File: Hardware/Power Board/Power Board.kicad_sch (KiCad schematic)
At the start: 15 parts, among them IC1 SN6507DGQR, T1 782100_35JVC

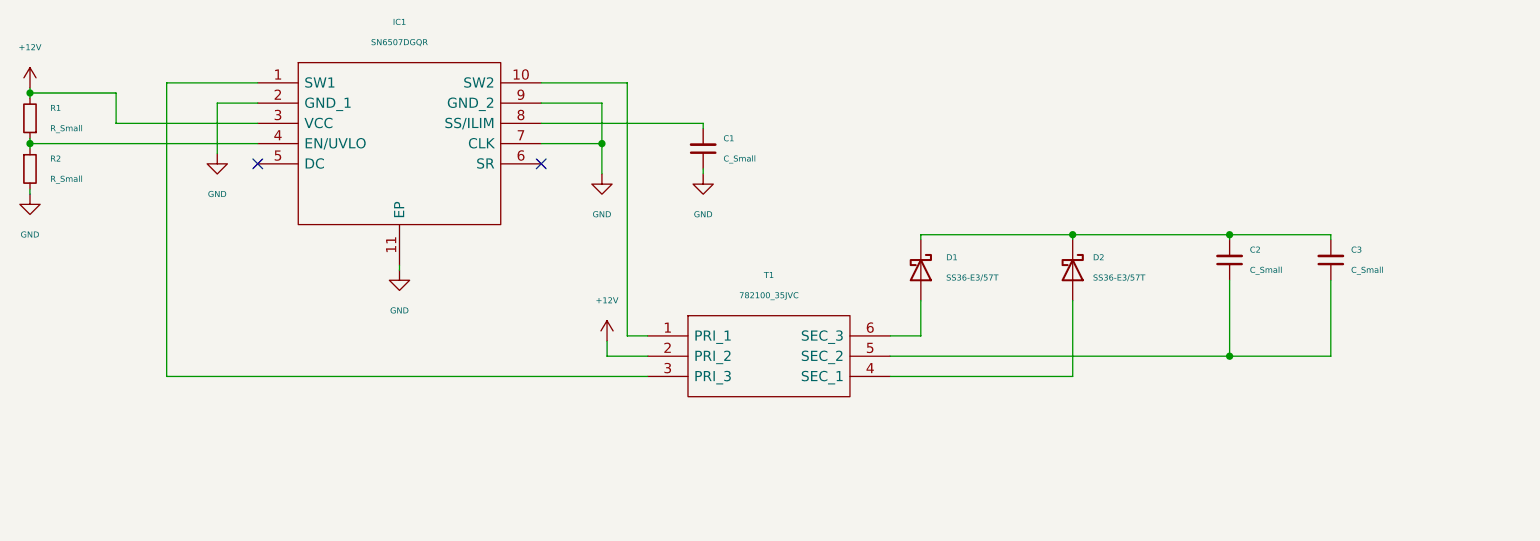
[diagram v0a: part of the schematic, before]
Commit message: Updates to board, changed gate driver IC to one with external clamp
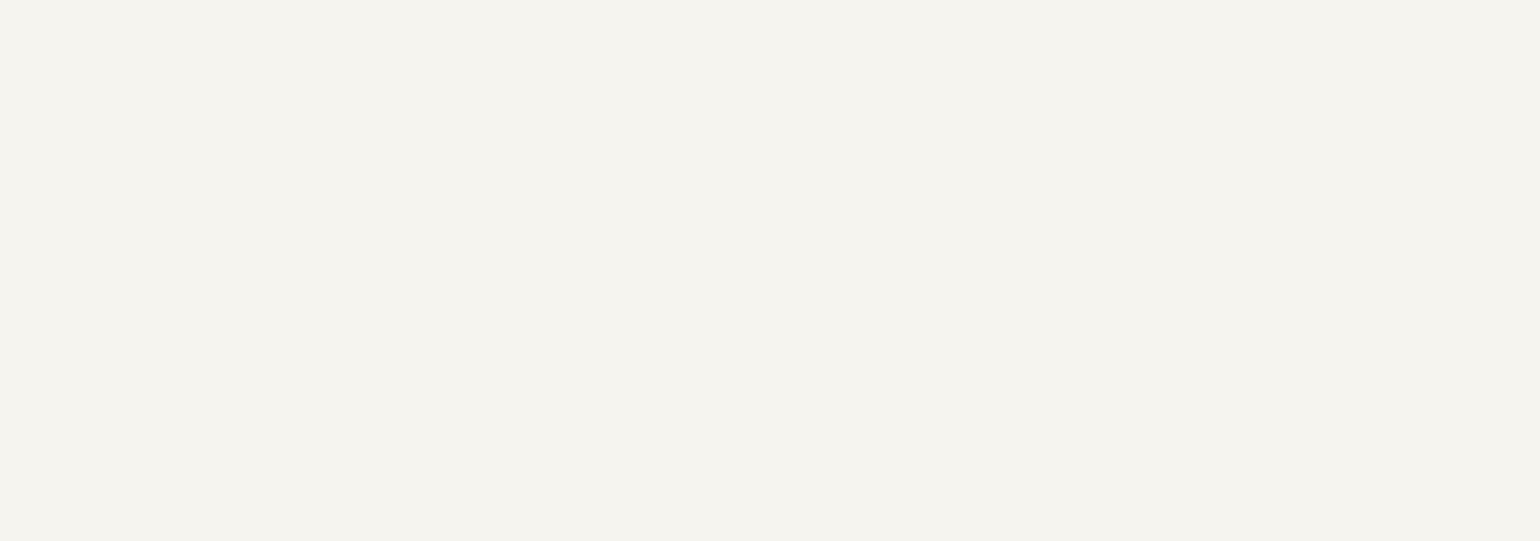
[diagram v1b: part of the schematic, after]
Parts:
- removed C1, C2, C3: C_Small, symbol Device:C_Small
- removed D1, D2: SS36-E3/57T, Diode_SMD:D_SMC, symbol Device:D_Schottky
- removed IC1: SN6507DGQR, SOP50P490X110-11N, symbol SamacSys_Parts:SN6507DGQR
- removed R1, R2: R_Small, symbol Device:R_Small
- removed T1: 782100_35JVC, 78210035JVC, symbol SamacSys_Parts:782100_35JVC
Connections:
- no-connect marks 2 -> 0

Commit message: Ditched ASC
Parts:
- removed R3, R4, R5, R6, R7, R8: R_Small, symbol Device:R_Small
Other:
- sheet LOW_SIDE_POWER_STAGE renamed POWER_STAGE
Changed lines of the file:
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@@
     (company "Logan Rosenmayer")
-  )
-  (wire (pts (xy 71.755 260.985) (xy 71.755 262.255))
-    (stroke (width 0) (type default))
-  )
-  (wire (pts (xy 71.755 273.685) (xy 71.755 274.955))
-    (stroke (width 0) (type default))
-  )
-  (wire (pts (xy 71.755 254.635) (xy 71.755 255.905))
-    (stroke (width 0) (type default))
-  )
-  (wire (pts (xy 71.755 267.335) (xy 71.755 268.605))
-    (stroke (width 0) (type default))
-  )
-  (wire (pts (xy 71.755 248.285) (xy 71.755 249.555))
-    (stroke (width 0) (type default))
-  )
-  (global_label "HV +" (shape input) (at 71.755 243.205 90) (fields_autoplaced)
-    (effects (font (size 1.27 1.27)) (justify left))
-    (property "Intersheetrefs" "${INTERSHEET_REFS}" (at 71.6756 235.8329 90)
-      (effects (font (size 1.27 1.27)) (justify left) hide)
-    )
-  )
-  (global_label "HV -" (shape input) (at 71.755 280.035 270) (fields_autoplaced)
-    (effects (font (size 1.27 1.27)) (justify right))
-    (property "Intersheetrefs" "${INTERSHEET_REFS}" (at 71.6756 287.4071 90)
-      (effects (font (size 1.27 1.27)) (justify right) hide)
-    )
-  )
-  (symbol (lib_id "Device:R_Small") (at 71.755 258.445 180) (unit 1)
-    (in_bom yes) (on_board yes) (dnp no) (fields_autoplaced)
-    (property "Reference" "R5" (at 73.66 257.1749 0)
-      (effects (font (size 0.75 0.75)) (justify right))
-    )
-    (property "Value" "R_Small" (at 73.66 259.7149 0)
-      (effects (font (size 0.75 0.75)) (justify right))
-    )
-    (property "Footprint" "" (at 71.755 258.445 0)
-      (effects (font (size 1.27 1.27)) hide)
-    )
-    (property "Datasheet" "~" (at 71.755 258.445 0)
-      (effects (font (size 1.27 1.27)) hide)
-    )
-    (pin "1")
-    (pin "2")
-    (instances
-      (project "Power Board"
-        (path "/6be5afcf-5319-4edd-874e-36cb4fffe262"
-          (reference "R5") (unit 1)
-        )
-      )
-    )
-  )
-  (symbol (lib_id "Device:R_Small") (at 71.755 252.095 180) (unit 1)
-    (in_bom yes) (on_board yes) (dnp no) (fields_autoplaced)
-    (property "Reference" "R4" (at 73.66 250.8249 0)
-      (effects (font (size 0.75 0.75)) (justify right))
-    )
-    (property "Value" "R_Small" (at 73.66 253.3649 0)
-      (effects (font (size 0.75 0.75)) (justify right))
-    )
-    (property "Footprint" "" (at 71.755 252.095 0)
-      (effects (font (size 1.27 1.27)) hide)
-    )
-    (property "Datasheet" "~" (at 71.755 252.095 0)
-      (effects (font (size 1.27 1.27)) hide)
-    )
-    (pin "1")
-    (pin "2")
-    (instances
-      (project "Power Board"
-        (path "/6be5afcf-5319-4edd-874e-36cb4fffe262"
-          (reference "R4") (unit 1)
-        )
-      )
-    )
-  )
-  (symbol (lib_id "Device:R_Small") (at 71.755 245.745 180) (unit 1)
-    (in_bom yes) (on_board yes) (dnp no) (fields_autoplaced)
-    (property "Reference" "R3" (at 73.66 244.4749 0)
-      (effects (font (size 0.75 0.75)) (justify right))
-    )
-    (property "Value" "R_Small" (at 73.66 247.0149 0)
-      (effects (font (size 0.75 0.75)) (justify right))
-    )
-    (property "Footprint" "" (at 71.755 245.745 0)
-      (effects (font (size 1.27 1.27)) hide)
-    )
-    (property "Datasheet" "~" (at 71.755 245.745 0)
-      (effects (font (size 1.27 1.27)) hide)
-    )
-    (pin "1")
-    (pin "2")
-    (instances
-      (project "Power Board"
-        (path "/6be5afcf-5319-4edd-874e-36cb4fffe262"
-          (reference "R3") (unit 1)
-        )
-      )
-    )
-  )
-  (symbol (lib_id "Device:R_Small") (at 71.755 277.495 180) (unit 1)
-    (in_bom yes) (on_board yes) (dnp no) (fields_autoplaced)
-    (property "Reference" "R8" (at 74.295 276.2249 0)
-      (effects (font (size 0.75 0.75)) (justify right))
-    )
-    (property "Value" "R_Small" (at 74.295 278.7649 0)
-      (effects (font (size 0.75 0.75)) (justify right))
-    )
-    (property "Footprint" "" (at 71.755 277.495 0)
-      (effects (font (size 1.27 1.27)) hide)
-    )
-    (property "Datasheet" "~" (at 71.755 277.495 0)
-      (effects (font (size 1.27 1.27)) hide)
-    )
-    (pin "1")
-    (pin "2")
-    (instances
-      (project "Power Board"
-        (path "/6be5afcf-5319-4edd-874e-36cb4fffe262"
-          (reference "R8") (unit 1)
-        )
-      )
-    )
-  )
-  (symbol (lib_id "Device:R_Small") (at 71.755 271.145 180) (unit 1)
-    (in_bom yes) (on_board yes) (dnp no) (fields_autoplaced)
-    (property "Reference" "R7" (at 73.66 269.8749 0)
-      (effects (font (size 0.75 0.75)) (justify right))
-    )
-    (property "Value" "R_Small" (at 73.66 272.4149 0)
-      (effects (font (size 0.75 0.75)) (justify right))
-    )
-    (property "Footprint" "" (at 71.755 271.145 0)
-      (effects (font (size 1.27 1.27)) hide)
-    )
-    (property "Datasheet" "~" (at 71.755 271.145 0)
-      (effects (font (size 1.27 1.27)) hide)
-    )
-    (pin "1")
-    (pin "2")
-    (instances
-      (project "Power Board"
-        (path "/6be5afcf-5319-4edd-874e-36cb4fffe262"
-          (reference "R7") (unit 1)
-        )
-      )
-    )
-  )
-  (symbol (lib_id "Device:R_Small") (at 71.755 264.795 180) (unit 1)
-    (in_bom yes) (on_board yes) (dnp no) (fields_autoplaced)
-    (property "Reference" "R6" (at 73.66 263.5249 0)
-      (effects (font (size 0.75 0.75)) (justify right))
-    )
-    (property "Value" "R_Small" (at 73.66 266.0649 0)
-      (effects (font (size 0.75 0.75)) (justify right))
-    )
-    (property "Footprint" "" (at 71.755 264.795 0)
-      (effects (font (size 1.27 1.27)) hide)
-    )
-    (property "Datasheet" "~" (at 71.755 264.795 0)
-      (effects (font (size 1.27 1.27)) hide)
-    )
-    (pin "1")
-    (pin "2")
-    (instances
-      (project "Power Board"
-        (path "/6be5afcf-5319-4edd-874e-36cb4fffe262"
-          (reference "R6") (unit 1)
-        )
-      )
-    )
   )
   (sheet (at 200.66 203.2) (size 42.545 30.48) (fields_autoplaced)
     (stroke (width 0.1524) (type solid))
     (fill (color 0 0 0 0.0000))
-    (property "Sheetname" "LOW_SIDE_POWER_STAGE" (at 200.66 202.4884 0)
+    (property "Sheetname" "POWER_STAGE" (at 200.66 202.4884 0)
       (effects (font (size 1.27 1.27)) (justify left bottom))
     )

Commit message: Board Layout Almost Done, about to remove Kelvin source due to concerns about uneven current sharing
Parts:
- added C153, C154, C155, C156, C157, C158, C159, C160: 100uF-420V-20%-D16P7.5, Capacitor_THT:CP_Radial_D16.0mm_P7.50mm, symbol Device:C_Polarized
- added C51 (x3), C54 (x3), C57 (x3), C60 (x3), C62 (x3), C65 (x3): 10uF-100V-10%-2220, Capacitor_SMD:C_2220_5650Metric, symbol Device:C_Small
- added C58 (x8): 1nF-50V-10%-0603, Capacitor_SMD:C_0603_1608Metric, symbol Device:C_Small
- added C58 (x3): 100nF-50V-10%-0603, Capacitor_SMD:C_0603_1608Metric, symbol Device:C_Small
- added D38, D5, D75: SS36-E3/57T, Diode_SMD:D_SMC, symbol Device:D_Schottky
- added H1, H2, H3, H4, H5, H6, H7, H8: MountingHole_Pad, MountingHole:MountingHole_3.2mm_M3_Pad_TopOnly, symbol Mechanical:MountingHole_Pad
- added J1, J2, J3, J4, J5: Screw_Terminal_01x01, _Home_Grow:ACTB273-Cu-T2, symbol Connector:Screw_Terminal_01x01
- added Q1: NJFET_Test shape for LV fet, Library:HYG050N13NS1B6, symbol Simulation_SPICE:NJFET
- added U14, U15, U16: HO_150-PW-0000, HO150PW0000, symbol SamacSys_Parts:HO_150-PW-0000
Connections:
- new net: C58.2, H7.1
- new net: C58.2, H4.1
- new net: C58.2, H2.1
- new net: C58.2, H6.1
- new net: C58.2, H1.1
- new net: C58.2, H5.1
- new net: C58.2, H8.1
- new net: C58.2, H3.1
- new net +5V: C58.2, C58.2, C58.2, U14.7 (+UC), U15.7 (+UC), U16.7 (+UC)
- new net A__CURRENT_CLK: U16.5 (P1)
- new net A__CURRENT_DOUT: U16.6 (P2)
- new net A__OCD: U16.1 (OCD)
- new net B__CURRENT_CLK: U15.5 (P1)
- new net B__CURRENT_DOUT: U15.6 (P2)
- new net B__OCD: U15.1 (OCD)
- new net C__CURRENT_CLK: U14.5 (P1)
- new net C__CURRENT_DOUT: U14.6 (P2)
- new net C__OCD: U14.1 (OCD)
- new net GND: C58.1, C58.1, C58.1, C58.1, C58.1, C58.1, C58.1, C58.1, C58.1, C58.1, C58.1, U14.8 (GND), U15.8 (GND), U16.8 (GND)
- new net GNDPWR: C153.2, C154.2, C155.2, C156.2, C157.2, C158.2, C159.2, C160.2, C51.2, C51.2, C51.2, C54.2, C54.2, C54.2, C57.2, C57.2, C57.2, C60.2, C60.2, C60.2, C62.2, C62.2, C62.2, C65.2, C65.2, C65.2, J4.1 (Pin_1)
- new net HV_SESNE/ISO_15V: D38.1 (K), D5.1 (K), D75.1 (K)
- new net PHASE_A: J5.1 (Pin_1)
- new net PHASE_B: J3.1 (Pin_1)
- new net PHASE_C: J1.1 (Pin_1)
- new net POWERSTAGE_A_LS/ISO_15V: D5.2 (A)
- new net POWERSTAGE_A_LS1/ISO_15V: D38.2 (A)
- new net POWERSTAGE_A_LS2/ISO_15V: D75.2 (A)
- new net VBUS: C153.1, C154.1, C155.1, C156.1, C157.1, C158.1, C159.1, C160.1, C51.1, C51.1, C51.1, C54.1, C54.1, C54.1, C57.1, C57.1, C57.1, C60.1, C60.1, C60.1, C62.1, C62.1, C62.1, C65.1, C65.1, C65.1, J2.1 (Pin_1)
- no-connect marks 0 -> 30
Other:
- removed sheet POWER_STAGE
- added sheet POWERSTAGE_A_HS (LS_PWR_STAGE.kicad_sch)
- added sheet POWERSTAGE_A_HS1 (LS_PWR_STAGE.kicad_sch)
- added sheet POWERSTAGE_A_HS2 (LS_PWR_STAGE.kicad_sch)
- added sheet POWERSTAGE_A_LS (LS_PWR_STAGE.kicad_sch)
- added sheet POWERSTAGE_A_LS1 (LS_PWR_STAGE.kicad_sch)
- added sheet POWERSTAGE_A_LS2 (LS_PWR_STAGE.kicad_sch)
- sheet HV_SESNE ports: added DIN, DOUT, HV_IN0+, HV_IN0-, HV_IN1+, HV_IN1-, HV_IN2+, HV_IN2-, HV_IN3+, HV_IN3-, HV_IN4+, HV_IN4-, HV_IN5+, HV_IN5-, HV_IN6+, HV_IN6-, HV_IN7+, HV_IN7-, ISO_0V, ISO_15V, SCLK, nCS, nDRDY, nRESET; removed none

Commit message: Finished intial LV board connector routing, going to tear up current sense and redo
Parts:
- removed Q1: NJFET_Test shape for LV fet, Library:HYG050N13NS1B6, symbol Simulation_SPICE:NJFET
- added J6, J7: 68712414022, 68712414022, symbol SamacSys_Parts:68712414022
- renumbered J5 to J1, J3 to J2, J1 to J3, J2 to J4, J4 to J5
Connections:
- net +3.3V: now also J6.22
- net +5V: now also J6.23
- net +9V: now also J7.11, J7.13, J7.15, J7.17
- net A__CURRENT_CLK: now also J7.12
- net A__CURRENT_DOUT: now also J7.14
- net A__OCD: now also J7.8
- net B__CURRENT_CLK: now also J7.16
- net B__CURRENT_DOUT: now also J7.18
- net B__OCD: now also J7.9
- net C__CURRENT_CLK: now also J7.20
- net C__CURRENT_DOUT: now also J7.22
- net C__OCD: now also J7.10
- net GND: now also J6.1, J6.24, J6.25, J6.26, J7.1, J7.19, J7.21, J7.23, J7.24, J7.25, J7.26
- new net ADC_RDY: J7.6
- new net ADC_RESET: J7.5
- new net BRIDGE_EN: J6.2
- new net DC/DC_EN: J6.3
- new net DIN: J7.4
- new net DOUT: J7.7
- new net FLT_HS_A: J6.19
- new net FLT_HS_B: J6.13
- new net FLT_HS_C: J6.7
- new net FLT_LS_A: J6.21
- new net FLT_LS_B: J6.15
- new net FLT_LS_C: J6.9
- new net PWM_HS_A: J6.16
- new net PWM_HS_B: J6.10
- new net PWM_HS_C: J6.4
- new net PWM_LS_A: J6.17
- new net PWM_LS_B: J6.11
- new net PWM_LS_C: J6.5
- new net RDY_HS_A: J6.18
- new net RDY_HS_B: J6.12
- new net RDY_HS_C: J6.6
- new net RDY_LS_A: J6.20
- new net RDY_LS_B: J6.14
- new net RDY_LS_C: J6.8
- new net SCLK: J7.3
- new net nCS: J7.2

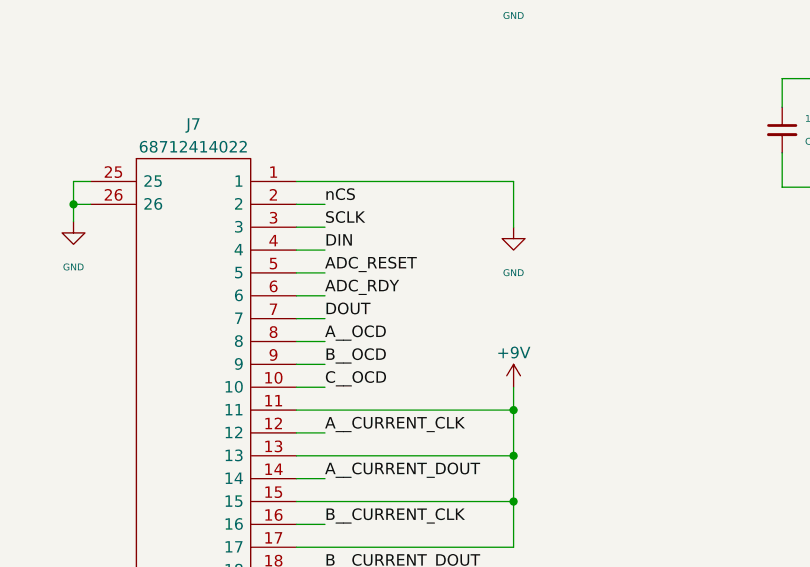
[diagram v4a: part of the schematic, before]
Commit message: Current sense reroute
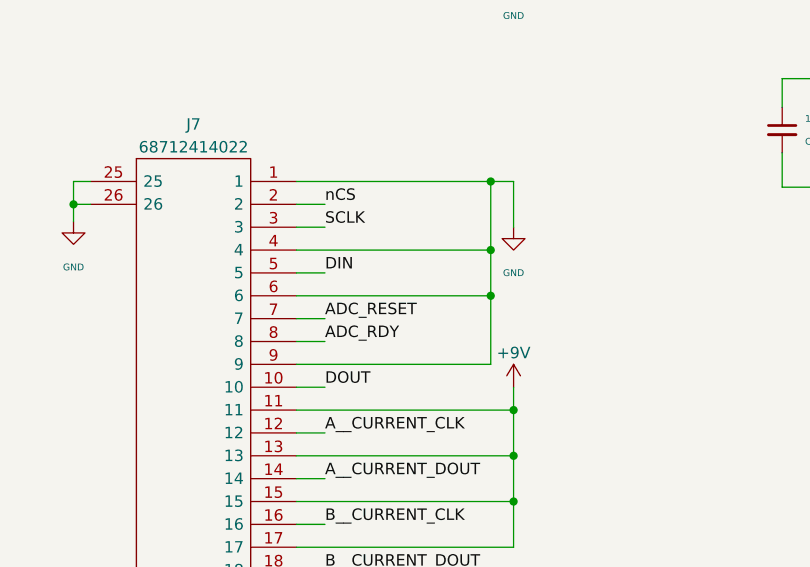
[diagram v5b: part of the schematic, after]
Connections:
- net ADC_RDY: now also J7.8; no longer J7.6
- net ADC_RESET: now also J7.7; no longer J7.5
- net A__OCD: no longer J7.8
- net B__OCD: no longer J7.9
- net C__OCD: no longer J7.10
- net DIN: now also J7.5; no longer J7.4
- net DOUT: now also J7.10; no longer J7.7
- net GND: now also J7.4, J7.6, J7.9
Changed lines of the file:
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@@
   (junction (at 364.49 252.73) (diameter 0) (color 0 0 0 0)
   )
+  (junction (at 287.655 168.275) (diameter 0) (color 0 0 0 0)
+  )
   (junction (at 364.49 264.795) (diameter 0) (color 0 0 0 0)
   )
@@
   (junction (at 373.38 35.56) (diameter 0) (color 0 0 0 0)
   )
+  (junction (at 287.655 155.575) (diameter 0) (color 0 0 0 0)
+  )
   (junction (at 387.35 99.695) (diameter 0) (color 0 0 0 0)
   )
@@
   )
   (junction (at 391.16 264.795) (diameter 0) (color 0 0 0 0)
+  )
+  (junction (at 287.655 163.195) (diameter 0) (color 0 0 0 0)
   )
   (junction (at 337.82 47.625) (diameter 0) (color 0 0 0 0)
@@
     (stroke (width 0) (type default))
   )
-  (wire (pts (xy 266.065 175.895) (xy 269.24 175.895))
+  (wire (pts (xy 266.065 175.895) (xy 287.655 175.895))
     (stroke (width 0) (type default))
   )
@@
     (stroke (width 0) (type default))
   )
-  (wire (pts (xy 266.065 155.575) (xy 290.195 155.575))
+  (wire (pts (xy 266.065 155.575) (xy 287.655 155.575))
     (stroke (width 0) (type default))
   )
@@
     (stroke (width 0) (type default))
   )
+  (wire (pts (xy 266.065 168.275) (xy 287.655 168.275))
+    (stroke (width 0) (type default))
+  )
   (wire (pts (xy 337.82 35.56) (xy 337.82 38.735))
     (stroke (width 0) (type default))
@@
     (stroke (width 0) (type default))
   )
-  (wire (pts (xy 266.065 168.275) (xy 269.24 168.275))
-    (stroke (width 0) (type default))
-  )
   (wire (pts (xy 266.065 203.835) (xy 269.24 203.835))
     (stroke (width 0) (type default))
@@
     (stroke (width 0) (type default))
   )
-  (wire (pts (xy 266.065 163.195) (xy 269.24 163.195))
+  (wire (pts (xy 266.065 163.195) (xy 287.655 163.195))
     (stroke (width 0) (type default))
   )
@@
     (stroke (width 0) (type default))
   )
+  (wire (pts (xy 287.655 168.275) (xy 287.655 163.195))
+    (stroke (width 0) (type default))
+  )
   (wire (pts (xy 266.065 183.515) (xy 269.24 183.515))
     (stroke (width 0) (type default))
@@
     (stroke (width 0) (type default))
   )
+  (wire (pts (xy 287.655 163.195) (xy 287.655 155.575))
+    (stroke (width 0) (type default))
+  )
+  (wire (pts (xy 287.655 175.895) (xy 287.655 168.275))
+    (stroke (width 0) (type default))
+  )
   (wire (pts (xy 243.205 155.575) (xy 241.3 155.575))
     (stroke (width 0) (type default))
@@
     (stroke (width 0) (type default))
   )
+  (wire (pts (xy 287.655 155.575) (xy 290.195 155.575))
+    (stroke (width 0) (type default))
+  )
   (wire (pts (xy 390.525 381) (xy 390.525 384.81))
     (stroke (width 0) (type default))
@@
     (effects (font (size 1.27 1.27)) (justify right bottom))
   )
-  (label "ADC_RESET" (at 269.24 165.735 0) (fields_autoplaced)
+  (label "ADC_RESET" (at 269.24 170.815 0) (fields_autoplaced)
     (effects (font (size 1.27 1.27)) (justify left bottom))
   )
@@
     (effects (font (size 1.27 1.27)) (justify right bottom))
   )
-  (label "B__OCD" (at 269.24 175.895 0) (fields_autoplaced)
-    (effects (font (size 1.27 1.27)) (justify left bottom))
-  )
   (label "FLT_HS_B" (at 269.24 99.06 0) (fields_autoplaced)
     (effects (font (size 1.27 1.27)) (justify left bottom))
@@
     (effects (font (size 1.27 1.27)) (justify right bottom))
   )
-  (label "DOUT" (at 269.24 170.815 0) (fields_autoplaced)
+  (label "DOUT" (at 269.24 178.435 0) (fields_autoplaced)
     (effects (font (size 1.27 1.27)) (justify left bottom))
   )
@@
     (effects (font (size 1.27 1.27)) (justify right bottom))
   )
-  (label "DIN" (at 269.24 163.195 0) (fields_autoplaced)
+  (label "DIN" (at 269.24 165.735 0) (fields_autoplaced)
     (effects (font (size 1.27 1.27)) (justify left bottom))
   )
@@
     (effects (font (size 1.27 1.27)) (justify right bottom))
   )
-  (label "A__OCD" (at 269.24 173.355 0) (fields_autoplaced)
-    (effects (font (size 1.27 1.27)) (justify left bottom))
-  )
   (label "SCLK" (at 335.915 353.695 180) (fields_autoplaced)
     (effects (font (size 1.27 1.27)) (justify right bottom))
@@
     (effects (font (size 1.27 1.27)) (justify right bottom))
   )
-  (label "C__OCD" (at 269.24 178.435 0) (fields_autoplaced)
-    (effects (font (size 1.27 1.27)) (justify left bottom))
-  )
   (label "PWM_LS_B" (at 335.915 177.165 180) (fields_autoplaced)
     (effects (font (size 1.27 1.27)) (justify right bottom))
@@
     (effects (font (size 1.27 1.27)) (justify right bottom))
   )
-  (label "ADC_RDY" (at 269.24 168.275 0) (fields_autoplaced)
-    (effects (font (size 1.27 1.27)) (justify left bottom))
-  )
+  (label "ADC_RDY" (at 269.24 173.355 0) (fields_autoplaced)
+    (effects (font (size 1.27 1.27)) (justify left bottom))
+  )
